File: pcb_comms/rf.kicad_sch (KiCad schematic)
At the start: 25 parts, among them IC4 BGS12WN6E6329XTSA1, J4 SMA_CONN

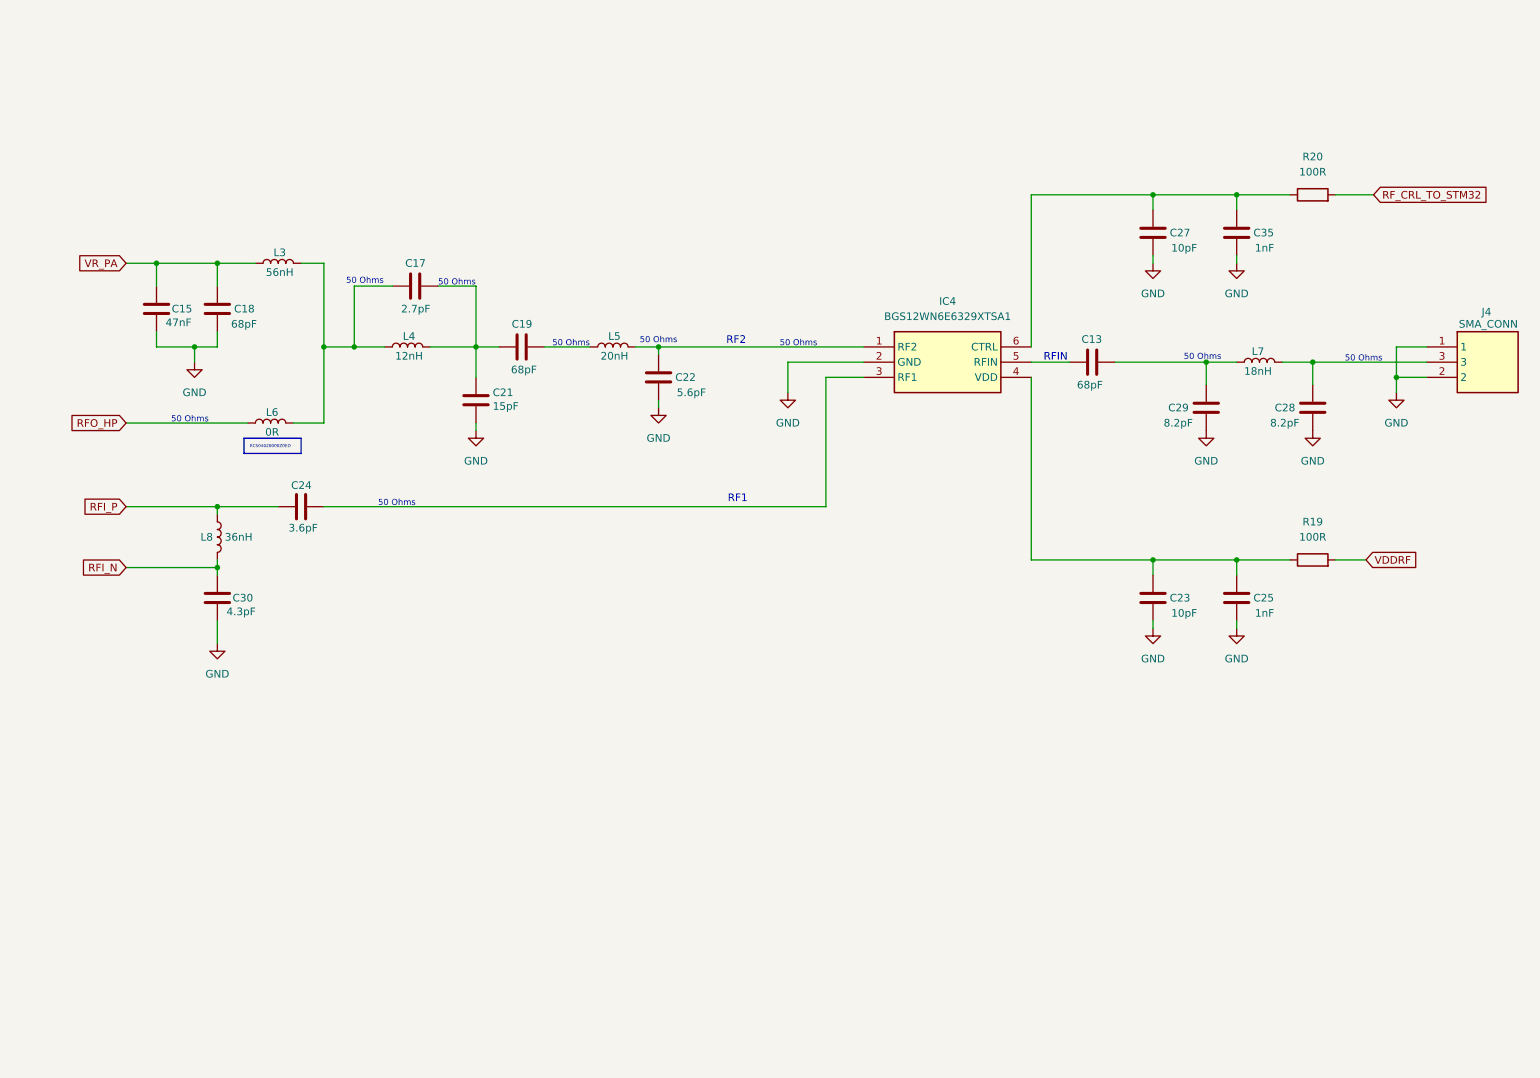
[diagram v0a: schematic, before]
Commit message: Add DRA818
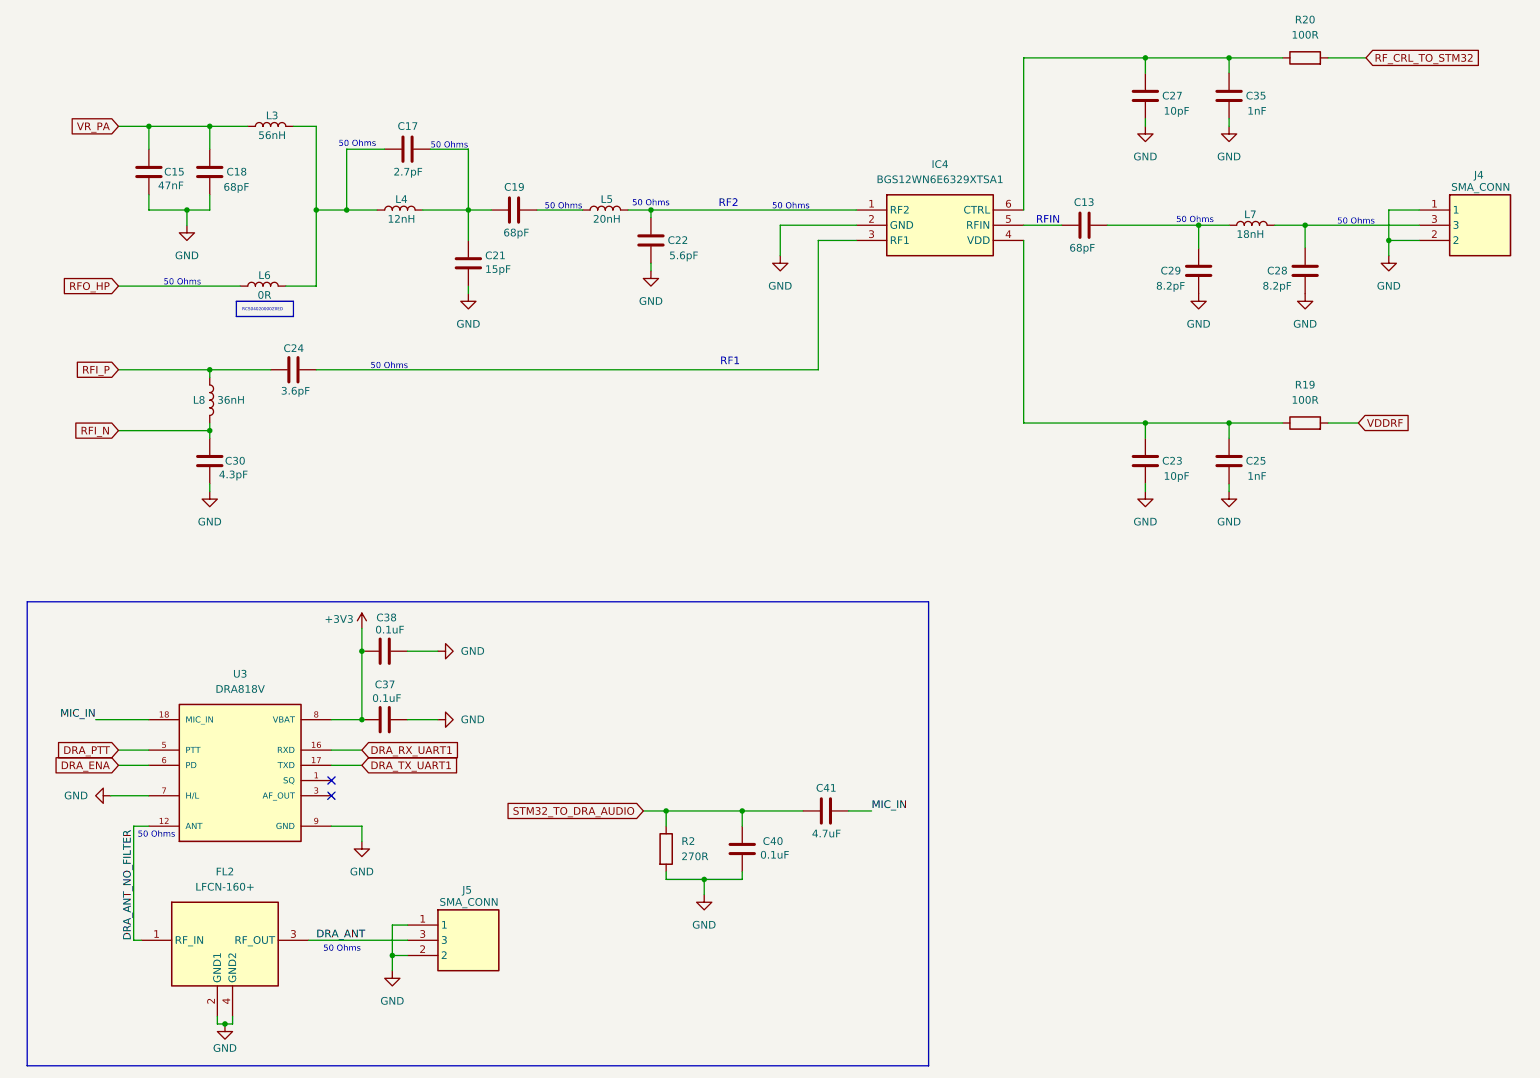
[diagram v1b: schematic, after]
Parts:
- added C37, C38, C40: 0.1uF, Capacitor_SMD:C_0805_2012Metric_Pad1.18x1.45mm_HandSolder, symbol Device:C
- added C41: 4.7uF, Capacitor_SMD:C_0805_2012Metric_Pad1.18x1.45mm_HandSolder, symbol Device:C
- added FL2: LFCN-160+, RF_FILTER_LFCN-160+:RF_FILTER_LFCN-160+, symbol RF_FILTER_LFCN-160+:LFCN-160+
- added J5: SMA_CONN, SMA_ANTENNA_CONSMA002-SMD-G:SMA_ANTENNA_CONSMA002-SMD-G, symbol SMA_ANTENNA_CONSMA002-SMD-G:CONSMA002-SMD-G
- added R2: 270R, Resistor_SMD:R_0805_2012Metric_Pad1.20x1.40mm_HandSolder, symbol Device:R
- added U3: DRA818V, DRA818V:DORJI_DRA818V, symbol DRA818V:DRA818V
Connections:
- net GND: now also C37.2, C38.2, C40.2, FL2.2 (GND1), FL2.4 (GND2), J5.1, J5.2, R2.2, U3.10 (GND), U3.7 (H/L), U3.9 (GND)
- new net +3V3: C37.1, C38.1, U3.8 (VBAT)
- new net DRA_ANT: FL2.3 (RF_OUT), J5.3
- new net DRA_ANT_NO_FILTER: FL2.1 (RF_IN), U3.12 (ANT)
- new net DRA_ENA: U3.6 (PD)
- new net DRA_PTT: U3.5 (PTT)
- new net DRA_RX_UART1: U3.16 (RXD)
- new net DRA_TX_UART1: U3.17 (TXD)
- new net MIC_IN: C41.2, U3.18 (MIC_IN)
- new net STM32_TO_DRA_AUDIO: C40.1, C41.1, R2.1
- no-connect marks 0 -> 2
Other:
- moved on the sheet: C13, C15, C17, C18, C19, C21, C22, C23, C24, C25, C27, C28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

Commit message: remove gps
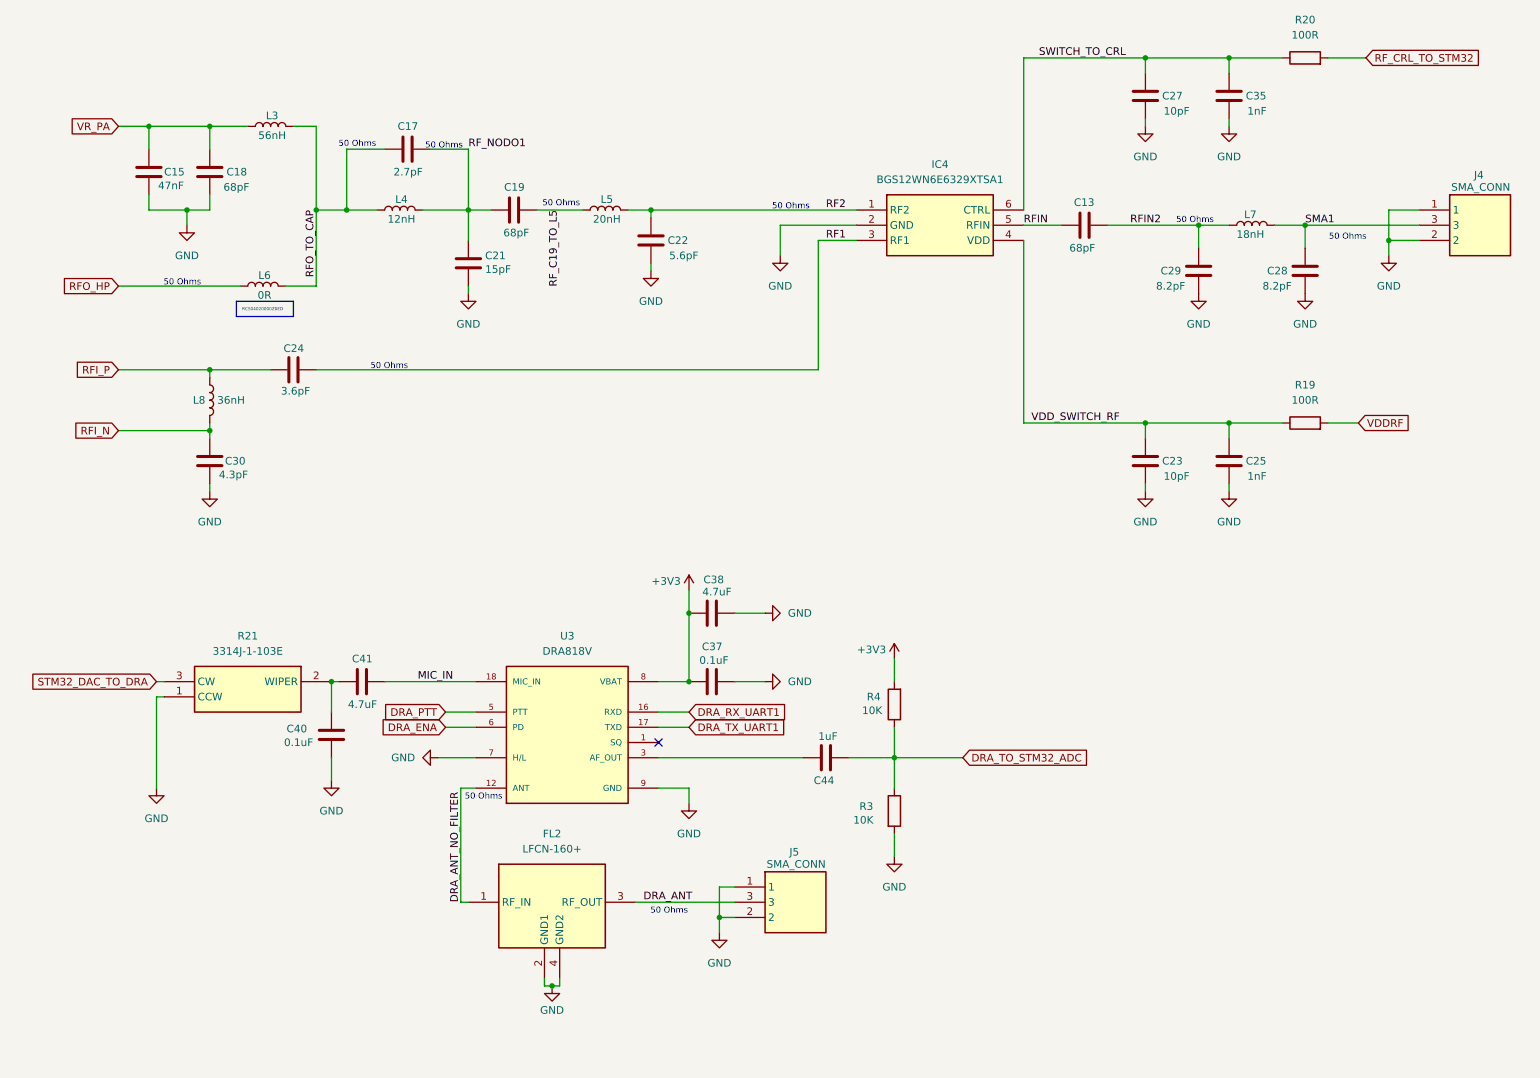
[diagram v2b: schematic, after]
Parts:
- removed R2: 270R, Resistor_SMD:R_0805_2012Metric_Pad1.20x1.40mm_HandSolder, symbol Device:R
- added C44: 1uF, Capacitor_SMD:C_0805_2012Metric_Pad1.18x1.45mm_HandSolder, symbol Device:C
- added R21: 3314J-1-103E, TRIMPOT_10K_3314J-1-103E:TRIMPOT_10K_3314J-1-103E, symbol TRIMPOT_10K_3314J-1-103E:3314J-1-103E
- added R3, R4: 10K, Resistor_SMD:R_0805_2012Metric_Pad1.20x1.40mm_HandSolder, symbol Device:R
- C38: value 0.1uF -> 4.7uF
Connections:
- net +3V3: now also R4.2
- net GND: now also R21.1 (CCW), R3.2
- net RF2: now reaches C22.1, IC4.1 (RF2), L5.2
- net RFO_TO_CAP: now reaches C17.1, L3.2, L4.1, L6.2
- net RF_NODO1: now reaches C17.2, C19.1, C21.1, L4.2
- net RF_C19_TO_L5: now reaches C19.2, L5.1
- net RF1: now reaches C24.2, IC4.3 (RF1)
- net VDD_SWITCH_RF: now reaches C23.1, C25.1, IC4.4 (VDD), R19.1
- net RFIN: now reaches C13.2, IC4.5 (RFIN)
- net SWITCH_TO_CRL: now reaches C27.1, C35.1, IC4.6 (CTRL), R20.1
- net at U3.3 (AF_OUT): now also C44.2
- net RFIN2: now reaches C13.1, C29.2, L7.2
- net SMA1: now reaches C28.2, J4.3, L7.1
- net STM32_TO_DRA_AUDIO: no longer names the net of C40.1, C41.1
- net STM32_TO_DRA_AUDIO: now also R21.2 (WIPER)
- new net DRA_TO_STM32_ADC: C44.1, R3.1, R4.1
- new net STM32_DAC_TO_DRA: R21.3 (CW)
- no-connect marks 2 -> 1
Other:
- note removed: "RF1"
- note removed: "RF2"
- note removed: "RFIN"
- moved on the sheet: C37, C38, C40, C41, FL2, J5, U3

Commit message: Update DRA
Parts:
- removed C37, C40: 0.1uF, Capacitor_SMD:C_0805_2012Metric_Pad1.18x1.45mm_HandSolder, symbol Device:C
- removed C38, C41: 4.7uF, Capacitor_SMD:C_0805_2012Metric_Pad1.18x1.45mm_HandSolder, symbol Device:C
- removed C44: 1uF, Capacitor_SMD:C_0805_2012Metric_Pad1.18x1.45mm_HandSolder, symbol Device:C
- removed FL2: LFCN-160+, RF_FILTER_LFCN-160+:RF_FILTER_LFCN-160+, symbol RF_FILTER_LFCN-160+:LFCN-160+
- removed J5: SMA_CONN, SMA_ANTENNA_CONSMA002-SMD-G:SMA_ANTENNA_CONSMA002-SMD-G, symbol SMA_ANTENNA_CONSMA002-SMD-G:CONSMA002-SMD-G
- removed R21: 3314J-1-103E, TRIMPOT_10K_3314J-1-103E:TRIMPOT_10K_3314J-1-103E, symbol TRIMPOT_10K_3314J-1-103E:3314J-1-103E
- removed R3, R4: 10K, Resistor_SMD:R_0805_2012Metric_Pad1.20x1.40mm_HandSolder, symbol Device:R
- removed U3: DRA818V, DRA818V:DORJI_DRA818V, symbol DRA818V:DRA818V
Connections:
- no-connect marks 1 -> 0

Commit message: Version 1.1
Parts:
- removed J4: SMA_CONN, SMA_ANTENNA_CONSMA002-SMD-G:SMA_ANTENNA_CONSMA002-SMD-G, symbol SMA_ANTENNA_CONSMA002-SMD-G:CONSMA002-SMD-G
- added J6: SMA_CONNECTOR, SMA_ANTENNA_VERTICAL:LPRS_SMA_CONNECTOR, symbol SMA_CONNECTOR:SMA_CONNECTOR
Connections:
- net GND: now also J6.G1, J6.G2, J6.G3, J6.G4
- net SMA1: now also J6.1
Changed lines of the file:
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@@
 		(color 0 0 0 0)
 	)
-	(junction
-		(at 250.19 57.15)
-		(diameter 0)
-		(color 0 0 0 0)
-	)
 	(wire
 		(pts
@@
 	(wire
 		(pts
-			(xy 236.22 54.61) (xy 255.27 54.61)
+			(xy 236.22 54.61) (xy 259.08 54.61)
 		)
 		(stroke
@@
 	(wire
 		(pts
-			(xy 255.27 52.07) (xy 250.19 52.07)
-		)
-		(stroke
-			(width 0)
-			(type default)
-		)
-	)
-	(wire
-		(pts
 			(xy 218.44 54.61) (xy 203.2 54.61)
 		)
@@
 	(wire
 		(pts
-			(xy 250.19 57.15) (xy 250.19 59.69)
+			(xy 254 57.15) (xy 254 59.69)
 		)
 		(stroke
@@
 	(wire
 		(pts
-			(xy 250.19 57.15) (xy 255.27 57.15)
+			(xy 254 57.15) (xy 259.08 57.15)
 		)
 		(stroke
@@
 	(wire
 		(pts
-			(xy 250.19 52.07) (xy 250.19 57.15)
-		)
-		(stroke
-			(width 0)
-			(type default)
-		)
-	)
-	(wire
-		(pts
 			(xy 223.52 36.83) (xy 223.52 38.1)
 		)
@@
 	(symbol
 		(lib_id "power:GND")
-		(at 250.19 59.69 0)
+		(at 254 59.69 0)
 		(mirror y)
 		(unit 1)
@@
 		(fields_autoplaced yes)
 		(property "Reference" "#PWR024"
-			(at 250.19 66.04 0)
+			(at 254 66.04 0)
 			(effects
 				(font
@@
 		)
 		(property "Value" "GND"
-			(at 250.19 64.77 0)
+			(at 254 64.77 0)
 			(effects
 				(font
@@
 		)
 		(property "Footprint" ""
-			(at 250.19 59.69 0)
+			(at 254 59.69 0)
 			(effects
 				(font
@@
 		)
 		(property "Datasheet" ""
-			(at 250.19 59.69 0)
+			(at 254 59.69 0)
 			(effects
 				(font
@@
 		)
 		(property "Description" "Power symbol creates a global label with name \"GND\" , ground"
-			(at 250.19 59.69 0)
+			(at 254 59.69 0)
 			(effects
 				(font
@@
 	)
 	(symbol
-		(lib_id "SMA_ANTENNA_CONSMA002-SMD-G:CONSMA002-SMD-G")
-		(at 255.27 52.07 0)
+		(lib_id "Device:C")
+		(at 96.52 60.96 0)
 		(unit 1)
 		(exclude_from_sim no)
@@
 		(on_board yes)
 		(dnp no)
-		(property "Reference" "J4"
-			(at 264.414 46.228 0)
+		(property "Reference" "C21"
+			(at 99.314 59.69 0)
 			(effects
 				(font
@@
 			)
 		)
-		(property "Value" "SMA_CONN"
-			(at 260.604 48.26 0)
+		(property "Value" "15pF"
+			(at 99.314 61.976 0)
 			(effects
 				(font
@@
 			)
 		)
-		(property "Footprint" "SMA_ANTENNA_CONSMA002-SMD-G:SMA_ANTENNA_CONSMA002-SMD-G"
-			(at 271.78 146.99 0)
+		(property "Footprint" "Capacitor_SMD:C_0805_2012Metric_Pad1.18x1.45mm_HandSolder"
+			(at 97.4852 64.77 0)
 			(effects
 				(font
 					(size 1.27 1.27)
 				)
-				(justify left top)
 				(hide yes)
 			)
 		)
-		(property "Datasheet" "https://www.te.com/commerce/DocumentDelivery/DDEController?Action=srchrtrv&DocNm=C-CONSMA002-SMD-X-X&DocType=Customer%20Drawing&DocLang=English&DocFormat=pdf&PartCntxt=CONSMA002-SMD-G"
-			(at 271.78 246.99 0)
+		(property "Datasheet" "~"
+			(at 96.52 60.96 0)
 			(effects
 				(font
 					(size 1.27 1.27)
 				)
-				(justify left top)
 				(hide yes)
 			)
 		)
-		(property "Description" "SMA Connector Receptacle, Female Socket 50 Ohms Surface Mount, Right Angle Solder"
-			(at 255.27 52.07 0)
+		(property "Description" "Unpolarized capacitor"
+			(at 96.52 60.96 0)
 			(effects
 				(font
@@
 			)
 		)
-		(property "Height" "10.9"
-			(at 271.78 446.99 0)
+		(property "KLC_S3.3" ""
+			(at 96.52 60.96 0)
 			(effects
 				(font
 					(size 1.27 1.27)
 				)
-				(justify left top)
 				(hide yes)
 			)
 		)
-		(property "Manufacturer_Name" "TE Connectivity"
-			(at 271.78 546.99 0)
+		(property "KLC_S4.1" ""
+			(at 96.52 60.96 0)
 			(effects
 				(font
 					(size 1.27 1.27)
 				)
-				(justify left top)
 				(hide yes)
 			)
 		)
-		(property "Manufacturer_Part_Number" "CONSMA002-SMD-G"
-			(at 271.78 646.99 0)
+		(pin "2"
+		)
+		(pin "1"
+		)
+		(instances
+			(project "pcb_comms_board"
+				(path "/ea597178-b44d-4db9-826c-8f86e8d231f0/f2ec5e10-3e2b-4fad-b66b-c622a3150eea"
+					(reference "C21")
+					(unit 1)
+				)
+			)
+		)
+	)
+	(symbol
+		(lib_id "SMA_CONNECTOR:SMA_CONNECTOR")
+		(at 261.62 54.61 0)
+		(mirror y)
+		(unit 1)
+		(exclude_from_sim no)
+		(in_bom yes)
+		(on_board yes)
+		(dnp no)
+		(property "Reference" "J6"
+			(at 262.6995 48.26 0)
 			(effects
 				(font
 					(size 1.27 1.27)
 				)
-				(justify left top)
-				(hide yes)
 			)
 		)
-		(property "Mouser Part Number" "712-CONSMA002-SMD-G"
-			(at 271.78 746.99 0)
+		(property "Value" "SMA_CONNECTOR"
+			(at 262.6995 50.8 0)
 			(effects
 				(font
 					(size 1.27 1.27)
 				)
-				(justify left top)
+			)
+		)
+		(property "Footprint" "SMA_ANTENNA_VERTICAL:LPRS_SMA_CONNECTOR"
+			(at 261.62 54.61 0)
+			(effects
+				(font
+					(size 1.27 1.27)
+				)
+				(justify bottom)
 				(hide yes)
 			)
 		)
-		(property "Mouser Price/Stock" "https://www.mouser.co.uk/ProductDetail/TE-Connectivity-Linx-Technologies/CONSMA002-SMD-G?qs=W0r2Z67sYIIuXfZnKPZ6sQ%3D%3D"
-			(at 271.78 846.99 0)
+		(property "Datasheet" ""
+			(at 261.62 54.61 0)
 			(effects
 				(font
 					(size 1.27 1.27)
 				)
-				(justify left top)
 				(hide yes)
 			)
 		)
-		(property "Arrow Part Number" "CONSMA002-SMD-G"
-			(at 271.78 946.99 0)
+		(property "Description" ""
+			(at 261.62 54.61 0)
 			(effects
 				(font
 					(size 1.27 1.27)
 				)
-				(justify left top)
 				(hide yes)
 			)
 		)
-		(property "Arrow Price/Stock" "https://www.arrow.com/en/products/consma002-smd-g/te-connectivity?utm_currency=USD&region=nac"
-			(at 271.78 1046.99 0)
+		(property "MF" "LPRS"
+			(at 261.62 54.61 0)
 			(effects
 				(font
 					(size 1.27 1.27)
 				)
-				(justify left top)
+				(justify bottom)
 				(hide yes)
 			)
 		)
-		(pin "3"
+		(property "MAXIMUM_PACKAGE_HEIGHT" "8.3 mm"
+			(at 261.62 54.61 0)
+			(effects
+				(font
+					(size 1.27 1.27)
+				)
+				(justify bottom)
+				(hide yes)
+			)
 		)
-		(pin "2"
+		(property "Package" "None"
+			(at 261.62 54.61 0)
+			(effects
+				(font
+					(size 1.27 1.27)
+				)
+				(justify bottom)
+				(hide yes)
+			)
 		)
-		(pin "1"
+		(property "Price" "None"
+			(at 261.62 54.61 0)
+			(effects
+				(font
+					(size 1.27 1.27)
+				)
+				(justify bottom)
+				(hide yes)
+			)
 		)
-		(instances
-			(project ""
-				(path "/ea597178-b44d-4db9-826c-8f86e8d231f0/f2ec5e10-3e2b-4fad-b66b-c622a3150eea"
-					(reference "J4")
-					(unit 1)
+		(property "Check_prices" "https://www.snapeda.com/parts/SMA%20CONNECTOR/LPRS/view-part/?ref=eda"
+			(at 261.62 54.61 0)
+			(effects
+				(font
+					(size 1.27 1.27)
 				)
+				(justify bottom)
+				(hide yes)
 			)
 		)
-	)
-	(symbol
-		(lib_id "Device:C")
-		(at 96.52 60.96 0)
-		(unit 1)
-		(exclude_from_sim no)
-		(in_bom yes)
-		(on_board yes)
-		(dnp no)
-		(property "Reference" "C21"
-			(at 99.314 59.69 0)
+		(property "STANDARD" "Manufacturer Recommendations"
+			(at 261.62 54.61 0)
 			(effects
 				(font
 					(size 1.27 1.27)
 				)
-				(justify left)
+				(justify bottom)
+				(hide yes)
 			)
 		)
-		(property "Value" "15pF"
-			(at 99.314 61.976 0)
+		(property "PARTREV" "1.3"
+			(at 261.62 54.61 0)
 			(effects
 				(font
 					(size 1.27 1.27)
 				)
-				(justify left)
+				(justify bottom)
+				(hide yes)
 			)
 		)
-		(property "Footprint" "Capacitor_SMD:C_0805_2012Metric_Pad1.18x1.45mm_HandSolder"
-			(at 97.4852 64.77 0)
+		(property "SnapEDA_Link" "https://www.snapeda.com/parts/SMA%20CONNECTOR/LPRS/view-part/?ref=snap"
+			(at 261.62 54.61 0)
 			(effects
 				(font
 					(size 1.27 1.27)
 				)
+				(justify bottom)
 				(hide yes)
 			)
 		)
-		(property "Datasheet" "~"
-			(at 96.52 60.96 0)
+		(property "MP" "SMA CONNECTOR"
+			(at 261.62 54.61 0)
 			(effects
 				(font
 					(size 1.27 1.27)
 				)
+				(justify bottom)
 				(hide yes)
 			)
 		)
-		(property "Description" "Unpolarized capacitor"
-			(at 96.52 60.96 0)
+		(property "Description_1" "RF Coaxial Straight SMA Connector"
+			(at 261.62 54.61 0)
 			(effects
 				(font
 					(size 1.27 1.27)
 				)
+				(justify bottom)
 				(hide yes)
 			)
 		)
-		(property "KLC_S3.3" ""
-			(at 96.52 60.96 0)
+		(property "Availability" "In Stock"
+			(at 261.62 54.61 0)
 			(effects
 				(font
 					(size 1.27 1.27)
 				)
+				(justify bottom)
 				(hide yes)
 			)
 		)
-		(property "KLC_S4.1" ""
-			(at 96.52 60.96 0)
+		(property "MANUFACTURER" "LPRS"
+			(at 261.62 54.61 0)
 			(effects
 				(font
 					(size 1.27 1.27)
 				)
+				(justify bottom)
 				(hide yes)
 			)
 		)
-		(pin "2"
+		(pin "G2"
+		)
+		(pin "G3"
 		)
 		(pin "1"
 		)
+		(pin "G1"
+		)
+		(pin "G4"
+		)
 		(instances
-			(project "pcb_comms_board"
+			(project ""
 				(path "/ea597178-b44d-4db9-826c-8f86e8d231f0/f2ec5e10-3e2b-4fad-b66b-c622a3150eea"
-					(reference "C21")
+					(reference "J6")
 					(unit 1)
 				)
